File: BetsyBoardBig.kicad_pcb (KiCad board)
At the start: 4 copper layers, 47 x 47 mm, 42 parts, among them J1 USB_B_Micro, J2 Micro_SD_Card, J3 Conn_02x06_Odd_Even, P1 VDD, P2 VBUS, P3 CORTEX-JTAG, P5 Digital, P6 BATT, P7 RTC, SW1 DIPSW, SW2 RST, U1 LP5907MFX-3.3, U2 USBLC6-2SC6, U3 APX823, U4 STM32L486Rx-LQFP64, U5 IS25WP256D-xM, X1 XTAL, Y1 Crystal

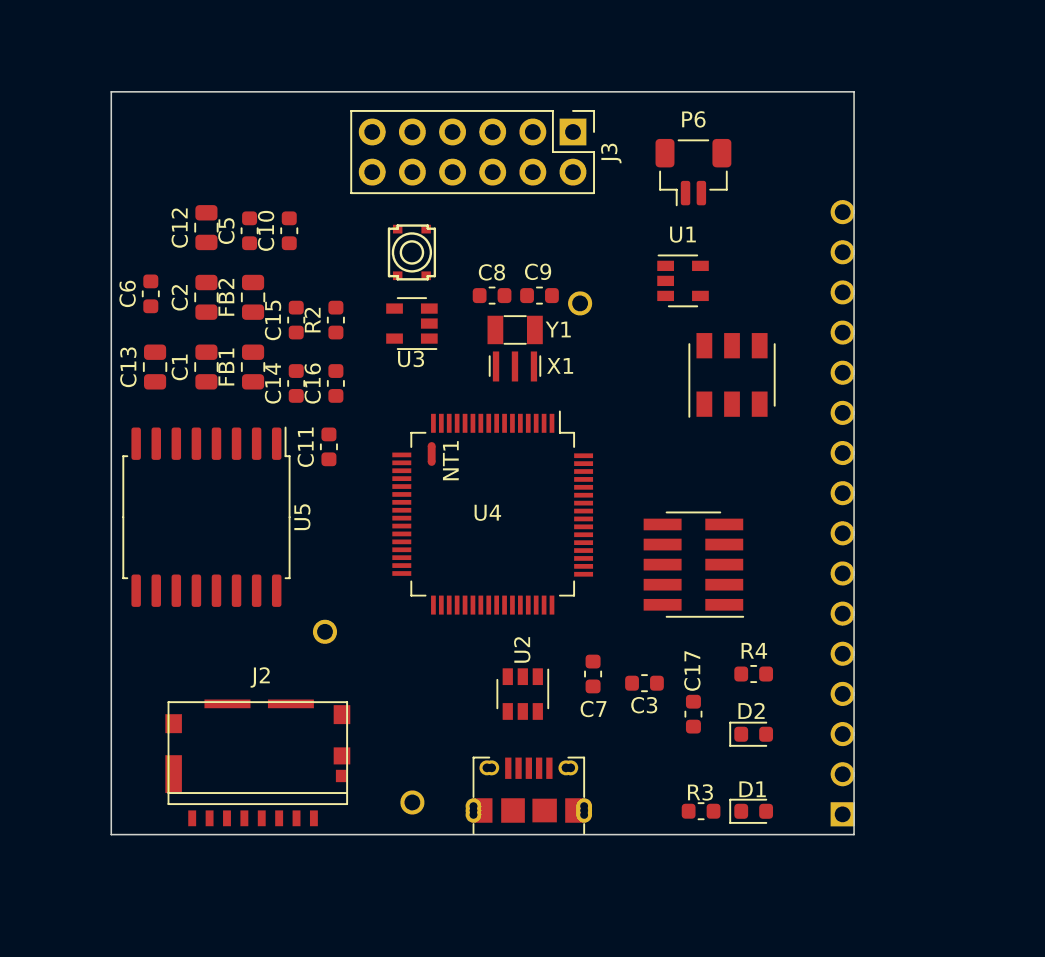
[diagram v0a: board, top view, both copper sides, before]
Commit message: Changes to the BBB.
- Fixing the QSPI_SCK problem.
- Cleaning up.
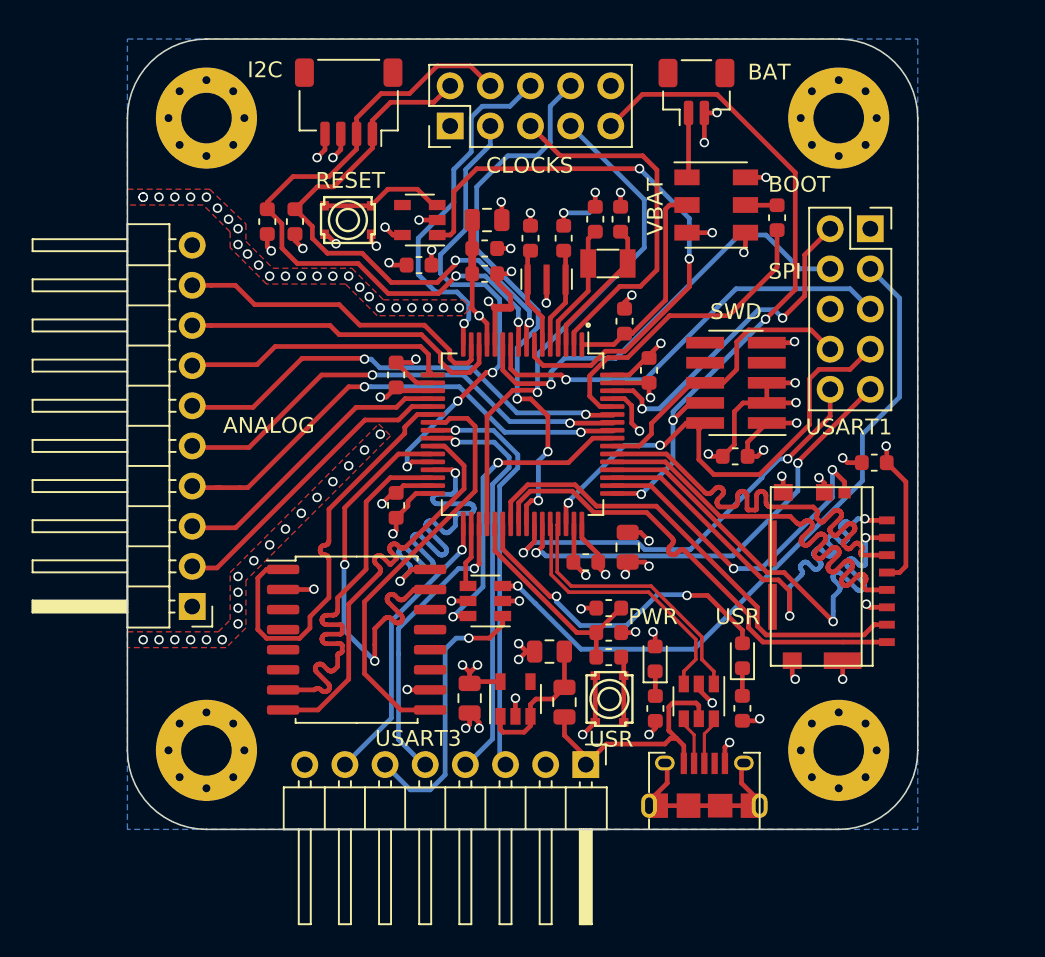
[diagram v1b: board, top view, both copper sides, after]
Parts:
- removed P1: VDD, engstad:pin-strip-1
- removed P2: VBUS, engstad:pin-strip-1
- removed P5: Digital, engstad:pin-strip-16
- removed P7: RTC, engstad:pin-socket-1
- added C18: 10pF, Capacitor_SMD:C_0603_1608Metric, F.Cu at (120.5, 62.6)
- added C4: 0.1uF, Capacitor_SMD:C_0603_1608Metric, F.Cu at (125.5, 87.5)
- added H1: Mounting, MountingHole:MountingHole_3.2mm_M3_Pad_Via, F.Cu at (100.0, 55.0)
- added H2: Mounting, MountingHole:MountingHole_3.2mm_M3_Pad_Via, F.Cu at (140.0, 55.0)
- added H3: Mounting, MountingHole:MountingHole_3.2mm_M3_Pad_Via, F.Cu at (140.0, 95.0)
- added H4: Mounting, MountingHole:MountingHole_3.2mm_M3_Pad_Via, F.Cu at (100.0, 95.0)
- added J4: USART3, Connector_PinHeader_2.54mm:PinHeader_1x08_P2.54mm_Horizontal, F.Cu at (124.0, 95.9)
- added J5: SPI/USART, Connector_PinSocket_2.54mm:PinSocket_2x05_P2.54mm_Vertical, F.Cu at (142.0, 62.0)
- added J6: I2C, Connector_JST:JST_SH_SM04B-SRSS-TB_1x04-1MP_P1.00mm_Horizontal, F.Cu at (109.0, 54.0)
- added J7: ANALOG, Connector_PinHeader_2.54mm:PinHeader_1x10_P2.54mm_Horizontal, F.Cu at (99.1, 85.9)
- added R1: 1K, Resistor_SMD:R_0603_1608Metric, F.Cu at (125.5, 89.1)
- added R5: 10K, Resistor_SMD:R_0603_1608Metric, F.Cu at (125.5, 86.0)
- added R6: 10K, Resistor_SMD:R_0603_1608Metric, F.Cu at (105.6, 61.5)
- added R7: 10K, Resistor_SMD:R_0603_1608Metric, F.Cu at (103.8, 61.5)
- added SW3: USR, engstad:tactile-switch-evpay-34x29mm, F.Cu at (125.5, 91.8)
- added U6: 74LVC1G3157, Package_TO_SOT_SMD:SOT-23-6, F.Cu at (117.7, 85.5)
- C13: value 1.0uF -> 10pF; footprint Capacitor_SMD:C_0805_2012Metric -> Capacitor_SMD:C_0603_1608Metric
- J1: footprint engstad:usb-micro-b-amphenol-fci-10118194 -> engstad:usb-micro-b-amphenol-fci-10118194-oval
- J3: value Conn_02x06_Odd_Even -> CLOCKS; footprint Connector_PinHeader_2.54mm:PinHeader_2x06_P2.54mm_Vertical -> Connector_PinHeader_2.54mm:PinHeader_2x05_P2.54mm_Vertical
- U4: footprint engstad:QFP-64_10x10_Pitch0.5mm -> Package_QFP:LQFP-64_10x10mm_P0.5mm
- moved J2 38.1 mm to (139.5, 84.0), turned to 90 degrees
- moved C11 34.5 mm to (142.2, 76.8), turned to 180 degrees
- moved C12 33.5 mm to (126.7, 82.2)
- moved C2 30.3 mm to (116.7, 91.7), turned to 270 degrees
- moved FB1 28.9 mm to (122.7, 92.0), turned to 270 degrees
- moved R2 28.7 mm to (136.1, 61.3), turned to 270 degrees
- moved U1 28.5 mm to (119.5, 91.8), turned to 90 degrees
- moved C1 28.2 mm to (121.7, 88.8), turned to 180 degrees
- moved C7 28.1 mm to (113.5, 64.3), turned to 180 degrees
- moved C13 27.1 mm to (122.6, 62.6)
- moved C10 22.0 mm to (126.5, 67.8)
- moved C17 21.9 mm to (128.0, 71.0)
- moved C6 21.2 mm to (117.6, 64.8), turned to 0 degrees
- moved C16 19.4 mm to (124.0, 83.1), turned to 180 degrees
- moved FB2 15.6 mm to (117.8, 61.5), turned to 0 degrees
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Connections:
- net /JTDO_SWO renamed /SWO
- net /JTMS_SWDIO renamed /SWDIO
- C11 pad 1: VDD -> VCC
- C12 pad 1: VDD -> VCC
- C13 pad 1: VDD -> /OSC_IN
- C14 pad 1: VDD -> VCC
- C15 pad 1: VDD -> VCC
- C16 pad 1: VDD -> VCC
- C17 pad 1: VDD -> VCC
- C2 pad 1: VDD -> VCC
- C3 pad 1: VDD -> VCC
- C7 pad 2: VDD -> VCC
- D1 pad 2: /D1 -> /LED_RED
- D2 pad 2: VDD -> VCC
- FB2 pad 2: VDD -> VCC
- J2 pad 4: VDD -> VCC
- J3 pad 1: /A1 -> VCC
- J3 pad 10: /A10 -> GND
- J3 pad 2: /A2 -> /I2C_SCL
- J3 pad 3: /A3 -> /RTC_OUT
- J3 pad 4: /A4 -> /I2C_SDA
- J3 pad 5: /A5 -> /RTC_TS
- J3 pad 6: /A6 -> /OCLK_LS
- J3 pad 7: /A7 -> /RTC_REFIN
- J3 pad 8: /A8 -> /OCLK_M
- J3 pad 9: /A9 -> /SWCLK
- P3 pad 1: VDD -> VCC
- P3 pad 10: /~JTRST -> Net-(P3-Pad10)
- P3 pad 4: /JTCK_SWCLK -> /SWCLK
- P3 pad 8: /JTDI -> Net-(P3-Pad8)
- SW1 pad 1: VDD -> /VBAT_IN
- SW1 pad 2: /BOOT_SEL -> /VBAT
- SW1 pad 3: GND -> VCC
- SW1 pad 4: /VBAT_IN -> VCC
- SW1 pad 5: /VBAT -> /BOOT_SEL
- SW1 pad 6: VDD -> GND
- U1 pad 5: VDD -> VCC
- U3 pad 5: VDD -> VCC
- U4 pad 10: /A3 -> /SPI2_MISO
- U4 pad 11: /A4 -> /SPI2_MOSI
- U4 pad 14: /A5 -> /OPAMP_IN+
- U4 pad 15: /A6 -> /OPAMP_IN-
- U4 pad 16: /A7 -> /OCLK_LS
- U4 pad 17: /A8 -> /OPAMP_OUT
- U4 pad 19: VDD -> VCC
- U4 pad 2: /RTC -> /RTC_TS
- U4 pad 20: /A9 -> /DAC_OUT1
- U4 pad 21: /A10 -> /DAC_OUT2
- U4 pad 24: /A11 -> /USART3_TXD
- U4 pad 25: /A12 -> /USART3_RXD
- U4 pad 28: /D1 -> /RTC_OUT
- U4 pad 32: VDD -> VCC
- U4 pad 33: /D4 -> /USART3_CK
- U4 pad 34: /D5 -> /PB13
- U4 pad 35: /D6 -> /USART3_RTS
- U4 pad 36: /D7 -> /RTC_REFIN
- U4 pad 37: /D8 -> /USR_SW
- U4 pad 38: /D9 -> /LED_RED
- U4 pad 41: /SDMMC_DET -> /OCLK_M
- U4 pad 42: /D10 -> /USART1_TX
- U4 pad 43: /D11 -> /USART1_RX
- U4 pad 48: VDD -> VCC
- U4 pad 49: /JTCK_SWCLK -> /SWCLK
- U4 pad 50: /JTDI -> /SDMMC_DET
- U4 pad 56: /~JTRST -> /SEL_USART3
- U4 pad 57: /D12 -> /COMP_OUT
- U4 pad 58: /D13 -> /COMP_IN+
- U4 pad 59: /D14 -> /COMP_IN-
- U4 pad 61: /D15 -> /USR
- U4 pad 62: /D16 -> /SPI2_SS#
- U4 pad 64: VDD -> VCC
- U4 pad 8: /A1 -> /I2C_SCL
- U4 pad 9: /A2 -> /I2C_SDA
- U5 pad 2: VDD -> VCC
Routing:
- net GND: track 0.00 -> 104.6 mm, vias 0 -> 44
- net VCC: track 0.00 -> 63.8 mm, vias 0 -> 23
- net /SPI2_SCK: track 0.00 -> 44.0 mm, vias 0 -> 1
- net /SWCLK: track 0.00 -> 43.3 mm, vias 0 -> 3
- net /I2C_SDA: track 0.00 -> 42.4 mm, vias 0 -> 2
- net /~RST: track 0.00 -> 37.7 mm, vias 0 -> 2
- net /OCLK_M: track 0.00 -> 35.5 mm, vias 0 -> 3
- net /I2C_SCL: track 0.00 -> 35.5 mm, vias 0 -> 2
- net /RTC_REFIN: track 0.00 -> 32.3 mm, vias 0 -> 1
- net /SWDIO: track 0.00 -> 30.9 mm, vias 0 -> 2
- net /COMP_OUT: track 0.00 -> 30.9 mm, vias 0 -> 2
- net /SDMMC_D2: track 0.00 -> 30.6 mm, vias 0 -> 2
- net /SDMMC_D0: track 0.00 -> 30.6 mm
- net /SDMMC_CMD: track 0.00 -> 30.5 mm
- net /SDMMC_D1: track 0.00 -> 30.5 mm
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- added copper zone on B.Cu, net GND
- added copper zone on Gnd.Cu, net GND
- added copper zone on Pow.Cu, net VCC
- added copper zone on Pow.Cu, net VDDA
- added copper zone on F.Cu, net VSSA
- added copper zone on Gnd.Cu, net VSSA
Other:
- board size 47 x 47 mm -> 50 x 50 mm
- net class Default: trace_width 0.25 -> 0.3
- net class PowerMain: trace_width 0.3 -> 0.4
- board text added: "ANALOG"
- board text added: "BAT"
- board text added: "BOOT"
- board text added: "CLOCKS"
- board text added: "I2C"
- board text added: "PWR"
- board text added: "RESET"
- board text added: "SPI"
- board text added: "SWD"
- board text added: "USART1"
- board text added: "USART3"
- board text added: "USR"
- board text added: "VBAT"

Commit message: Major changes due to mistakes
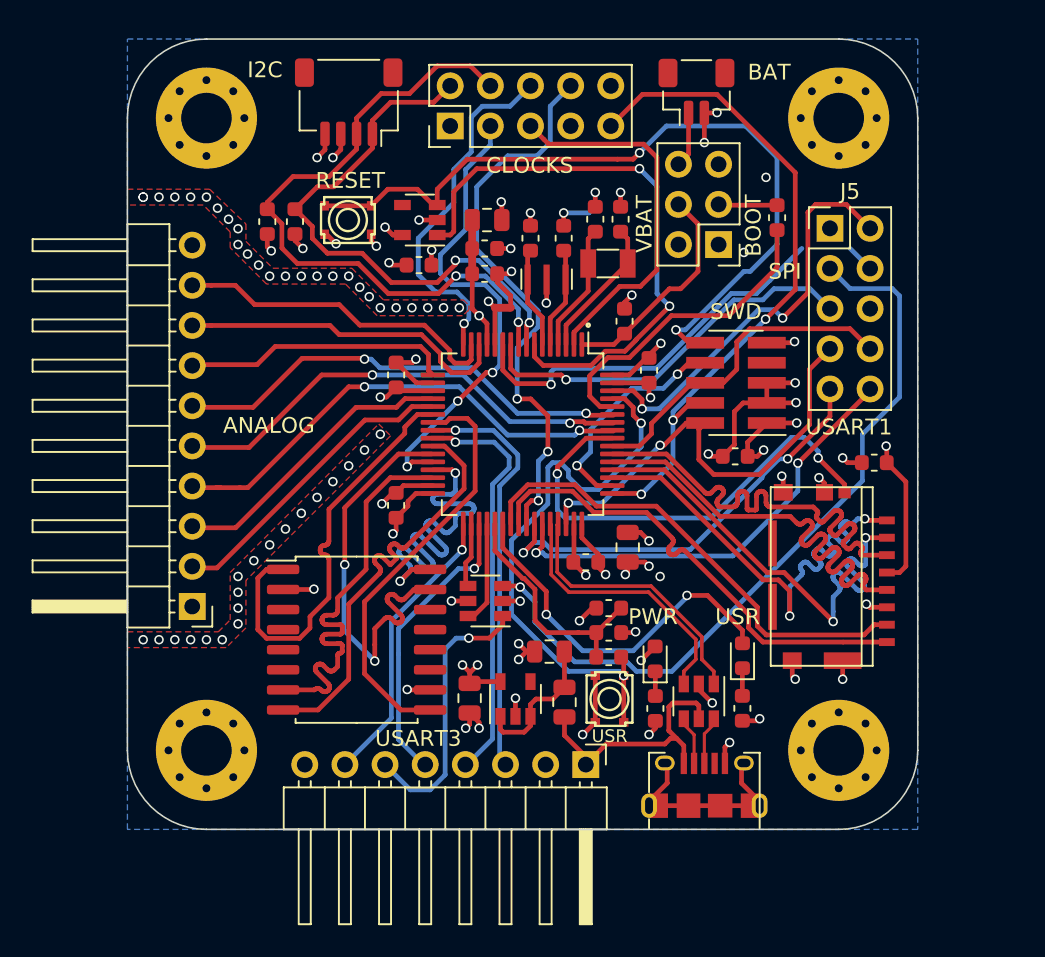
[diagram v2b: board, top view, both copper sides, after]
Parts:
- D2: value GREEN -> GRN
- J5: footprint Connector_PinSocket_2.54mm:PinSocket_2x05_P2.54mm_Vertical -> Connector_PinHeader_2.54mm:PinHeader_2x05_P2.54mm_Vertical
- SW1: value DIPSW -> JUMPER_x2; footprint engstad:slide-switch-smd-cas-220-d20 -> Connector_PinHeader_2.54mm:PinHeader_2x03_P2.54mm_Vertical
- U1: value LP5907MFX-3.3 -> TLV75733PDBVR‎
- moved J5 2.55 mm to (139.4, 62.0)
- moved SW1 2.50 mm to (132.4, 63.0), turned to 180 degrees
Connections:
- net /SWCLK renamed /SWCLK_JTCK
- net /SWDIO renamed /SWDIO_JTMS
- net /SWO renamed /SWO_JTDO
- C7 pad 1: GND -> VCC
- C7 pad 2: VCC -> GND
- J3 pad 7: /RTC_REFIN -> Net-(J3-Pad7)
- J5 pad 10: /USART1_TX -> /USART1_RX
- J5 pad 9: /USART1_RX -> /USART1_TX
- P3 pad 10: Net-(P3-Pad10) -> /RSTIN#
- P3 pad 8: Net-(P3-Pad8) -> /JTDI
- R1 pad 2: /BTN -> /USR_BTN
- SW1 pad 1: /VBAT_IN -> VCC
- SW1 pad 2: /VBAT -> VCC
- SW1 pad 3: VCC -> /BOOT_SEL
- SW1 pad 4: VCC -> /VBAT
- SW1 pad 5: /BOOT_SEL -> GND
- SW1 pad 6: GND -> /VBAT_IN
- SW2 pad 2: Net-(SW2-Pad2) -> /RSTIN#
- SW3 pad 2: /BTN -> /USR_BTN
- U3 pad 3: Net-(SW2-Pad2) -> /RSTIN#
- U4 pad 36: /RTC_REFIN -> /SEL_USART3
- U4 pad 50: /SDMMC_DET -> /JTDI
- U4 pad 56: /SEL_USART3 -> /SDMMC_DET
- U4 pad 61: /USR -> /USR_BTN
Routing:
- net /RSTIN#: track 0.00 -> 49.3 mm, vias 0 -> 2
- net /USR_BTN: track 0.00 -> 35.5 mm, vias 0 -> 2
- net /RTC_REFIN: track 32.3 -> 0.00 mm, vias 1 -> 0
- net GND: track 104.6 -> 88.9 mm, vias 44 -> 46
- net /JTDI: track 0.00 -> 14.4 mm, vias 0 -> 2
- net /SEL_USART3: track 19.8 -> 6.53 mm, vias 2 -> 0
- net Net-(SW2-Pad2): track 7.97 -> 0.00 mm
- net /SDMMC_DET: track 21.5 -> 29.5 mm
- net /SPI2_SS#: track 21.3 -> 26.5 mm
- net /SPI2_SCK: track 44.0 -> 48.6 mm
- net /BTN: track 4.19 -> 0.00 mm
- net /USR: track 3.22 -> 0.00 mm, vias 1 -> 0
- net /SWO_JTDO: track 18.7 -> 21.3 mm
- net /SPI2_MISO: track 27.5 -> 24.9 mm
- net VCC: track 63.8 -> 61.3 mm, vias 23 -> 21
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
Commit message: More changes.
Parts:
- moved NT1 0.59 mm to (118.4, 66.5), turned to 270 degrees
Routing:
- net /SPI2_MOSI: track 26.7 -> 29.6 mm
- net /RSTIN#: track 49.3 -> 47.9 mm
- net GND: track 88.9 -> 87.6 mm

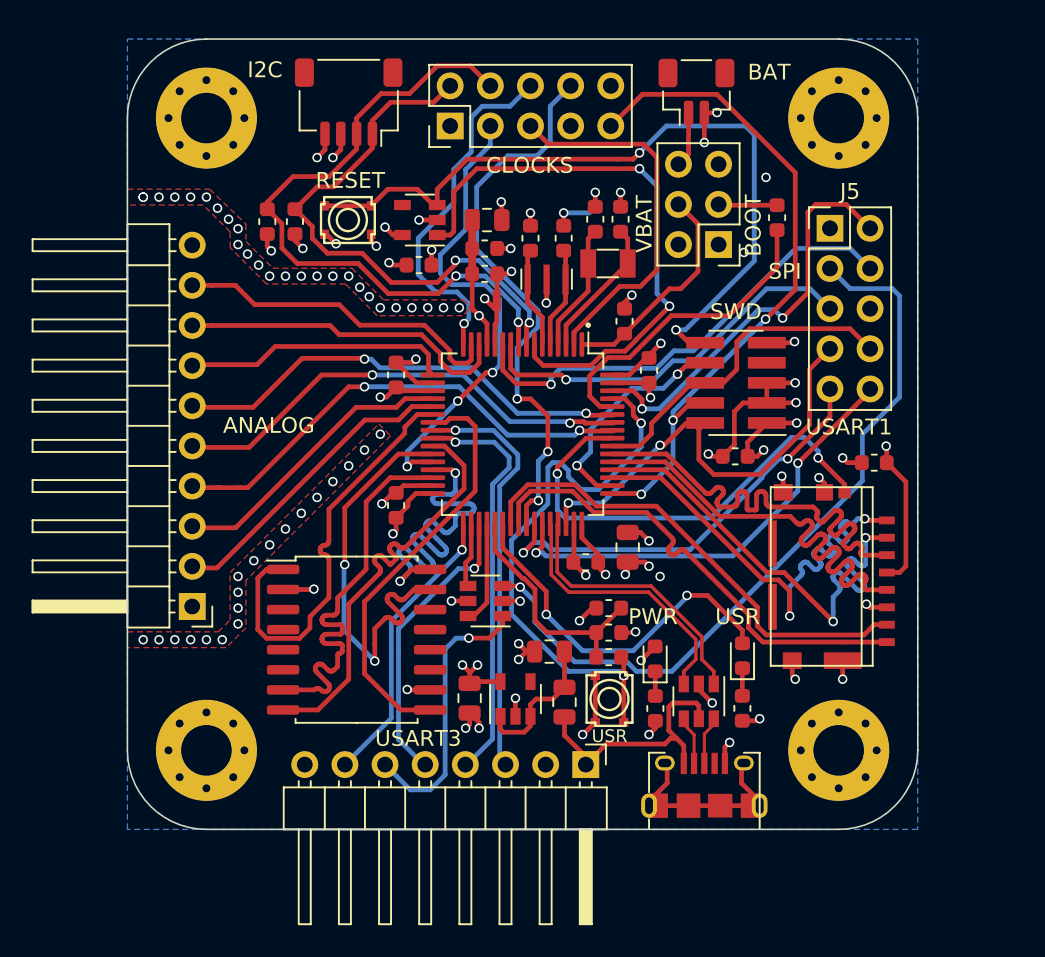
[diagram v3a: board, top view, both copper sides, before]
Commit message: Adding +5V support for I2C port, and fixing courtyard layer.
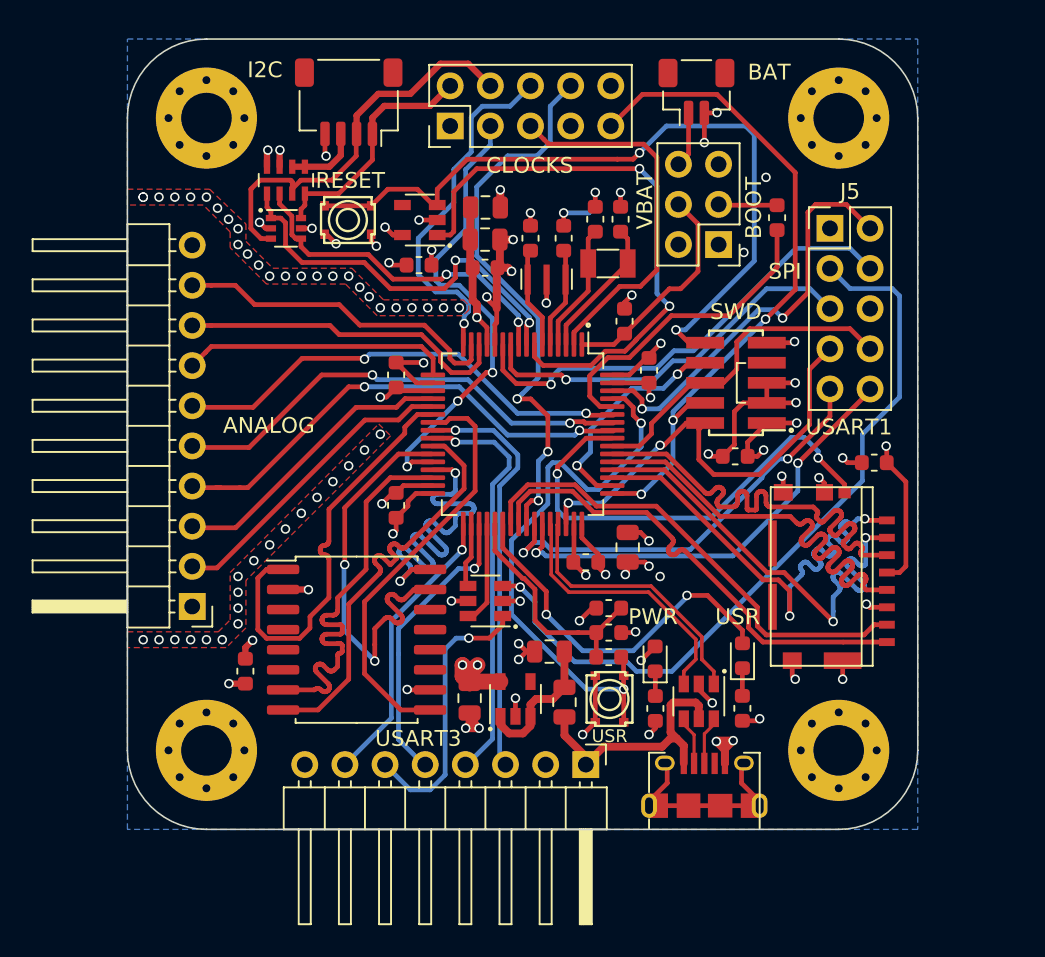
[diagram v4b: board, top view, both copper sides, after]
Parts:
- removed R6, R7: 10K, Resistor_SMD:R_0603_1608Metric
- added C19: 0.1uF, Capacitor_SMD:C_0603_1608Metric, F.Cu at (102.5, 90.0)
- added Q1: BSS138BKS, Package_TO_SOT_SMD:SOT-363_SC-70-6, F.Cu at (105.0, 62.0)
- added RN1: 10K, Resistor_SMD:R_Array_Concave_4x0603, F.Cu at (105.0, 58.9)
- C13, C18: value 10pF -> 16pF
- C5: footprint Capacitor_SMD:C_0603_1608Metric -> Capacitor_SMD:C_0805_2012Metric
- C8, C9: value 10pF -> 12pF
- R3, R4: value 470 -> 180
- moved FB2 0.80 mm to (117.7, 60.7)
- moved C5 0.56 mm to (117.6, 62.7)
- moved C6 0.39 mm to (117.6, 64.5)
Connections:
- J1 pad 4: Net-(J1-Pad4) -> (no net)
- J3 pad 2: /I2C_SCL -> /EXTSCL
- J3 pad 4: /I2C_SDA -> /EXTSDA
- J3 pad 7: Net-(J3-Pad7) -> (no net)
- J6 pad 1: /I2C_SCL -> /EXTSCL
- J6 pad 2: /I2C_SDA -> /EXTSDA
- J6 pad 3: VCC -> +5V
- P3 pad 7: Net-(P3-Pad7) -> (no net)
- U1 pad 4: Net-(U1-Pad4) -> (no net)
- U3 pad 4: Net-(U3-Pad4) -> (no net)
- U5 pad 11: Net-(U5-Pad11) -> (no net)
- U5 pad 12: Net-(U5-Pad12) -> (no net)
- U5 pad 13: Net-(U5-Pad13) -> (no net)
- U5 pad 14: Net-(U5-Pad14) -> (no net)
- U5 pad 3: Net-(U5-Pad3) -> (no net)
- U5 pad 4: Net-(U5-Pad4) -> (no net)
- U5 pad 5: Net-(U5-Pad5) -> (no net)
- U5 pad 6: Net-(U5-Pad6) -> (no net)
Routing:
- net /EXTSDA: track 0.00 -> 25.8 mm
- net /I2C_SDA: track 42.4 -> 21.8 mm
- net /EXTSCL: track 0.00 -> 15.2 mm
- net /I2C_SCL: track 35.5 -> 25.4 mm
- net VCC: track 61.3 -> 70.4 mm, vias 21 -> 23
- net GND: track 87.6 -> 93.2 mm, vias 46 -> 48
- net +5V: track 0.00 -> 4.73 mm
- net VDDA: track 8.26 -> 9.12 mm
- net /RTC_OUT: track 30.1 -> 29.4 mm
